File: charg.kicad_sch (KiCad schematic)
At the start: 21 parts, among them J1 Vbus, J2 GND, J3 Vout, J4 EN, Q1 FDC610PZ

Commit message: fixes
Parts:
- removed BT1: Battery_Cell, symbol Device:Battery_Cell
- added J?: Vbatt, symbol Connector_Generic:Conn_01x01
- C3, C5: footprint (none) -> capa 10uf:CAPAE530X610N
- TH1: footprint (none) -> Button_Switch_THT:KSA_Tactile_SPST
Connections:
- net at Battery_Charger_IC1.10 (BAT), C5.1, L1.2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: now also J?.1 (Pin_1)
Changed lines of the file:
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@@
   (junction (at 92.71 118.11) (diameter 0) (color 0 0 0 0)
   )
-  (junction (at 109.22 104.14) (diameter 0) (color 0 0 0 0)
-  )
-  (junction (at 194.31 114.3) (diameter 0) (color 0 0 0 0)
-  )
   (junction (at 102.87 104.14) (diameter 0) (color 0 0 0 0)
   )
@@
     (stroke (width 0) (type default) (color 0 0 0 0))
   )
-  (wire (pts (xy 194.31 111.76) (xy 194.31 114.3))
-    (stroke (width 0) (type default) (color 0 0 0 0))
-  )
   (wire (pts (xy 175.26 80.01) (xy 181.61 80.01))
     (stroke (width 0) (type default) (color 0 0 0 0))
@@
     (stroke (width 0) (type default) (color 0 0 0 0))
   )
-  (wire (pts (xy 113.03 104.14) (xy 109.22 104.14))
-    (stroke (width 0) (type default) (color 0 0 0 0))
-  )
   (wire (pts (xy 139.7 121.92) (xy 139.7 124.46))
     (stroke (width 0) (type default) (color 0 0 0 0))
@@
     (stroke (width 0) (type default) (color 0 0 0 0))
   )
-  (wire (pts (xy 180.34 100.33) (xy 180.34 104.14))
+  (wire (pts (xy 180.34 102.87) (xy 180.34 104.14))
     (stroke (width 0) (type default) (color 0 0 0 0))
   )
@@
     (stroke (width 0) (type default) (color 0 0 0 0))
   )
-  (wire (pts (xy 172.72 124.46) (xy 172.72 100.33))
+  (wire (pts (xy 172.72 124.46) (xy 172.72 102.87))
     (stroke (width 0) (type default) (color 0 0 0 0))
   )
@@
     (stroke (width 0) (type default) (color 0 0 0 0))
   )
-  (wire (pts (xy 194.31 104.14) (xy 194.31 96.52))
-    (stroke (width 0) (type default) (color 0 0 0 0))
-  )
-  (wire (pts (xy 172.72 100.33) (xy 180.34 100.33))
+  (wire (pts (xy 172.72 102.87) (xy 180.34 102.87))
     (stroke (width 0) (type default) (color 0 0 0 0))
   )
@@
       (effects (font (size 1.27 1.27)) (justify left))
     )
-    (property "Footprint" "" (id 2) (at 102.5652 73.66 0)
+    (property "Footprint" "capa 10uf:CAPAE530X610N" (id 2) (at 102.5652 73.66 0)
       (effects (font (size 1.27 1.27)) hide)
     )
@@
       (effects (font (size 1.27 1.27)) (justify left))
     )
-    (property "Footprint" "" (id 2) (at 180.34 109.22 0)
+    (property "Footprint" "Button_Switch_THT:KSA_Tactile_SPST" (id 2) (at 180.34 109.22 0)
       (effects (font (size 1.27 1.27)) hide)
     )
@@
     (pin "1")
     (pin "2")
+  )
+  (symbol (lib_name "Conn_01x01_2") (lib_id "Connector_Generic:Conn_01x01") (at 199.39 96.52 0) (unit 1)
+    (in_bom yes) (on_board yes)
+    (property "Reference" "J?" (id 0) (at 201.93 95.2499 0)
+      (effects (font (size 1.27 1.27)) (justify left) hide)
+    )
+    (property "Value" "Vbatt" (id 1) (at 203.2 96.52 0)
+      (effects (font (size 1.27 1.27)) (justify left))
+    )
+    (property "Footprint" "" (id 2) (at 199.39 96.52 0)
+      (effects (font (size 1.27 1.27)) hide)
+    )
+    (property "Datasheet" "~" (id 3) (at 199.39 96.52 0)
+      (effects (font (size 1.27 1.27)) hide)
+    )
+    (pin "1")
   )
   (symbol (lib_id "Device:C") (at 102.87 110.49 0) (unit 1)
@@
       (effects (font (size 1.27 1.27)) (justify left))
     )
-    (property "Footprint" "" (id 2) (at 182.5752 87.63 0)
+    (property "Footprint" "capa 10uf:CAPAE530X610N" (id 2) (at 182.5752 87.63 0)
       (effects (font (size 1.27 1.27)) hide)
     )
@@
     (pin "2")
   )
-  (symbol (lib_id "Device:Battery_Cell") (at 194.31 109.22 0) (unit 1)
-    (in_bom yes) (on_board yes)
-    (property "Reference" "BT1" (id 0) (at 198.12 105.9179 0)
-      (effects (font (size 1.27 1.27)) (justify left))
-    )
-    (property "Value" "Battery_Cell" (id 1) (at 196.85 109.22 0)
-      (effects (font (size 1.27 1.27)) (justify left))
-    )
-    (property "Footprint" "" (id 2) (at 194.31 107.696 90)
-      (effects (font (size 1.27 1.27)) hide)
-    )
-    (property "Datasheet" "~" (id 3) (at 194.31 107.696 90)
-      (effects (font (size 1.27 1.27)) hide)
-    )
-    (pin "1")
-    (pin "2")
-  )
   (symbol (lib_name "Conn_01x01_1") (lib_id "Connector_Generic:Conn_01x01") (at 86.36 118.11 180) (unit 1)
     (in_bom yes) (on_board yes)
@@
       (reference "#PWR?") (unit 1) (value "Earth") (footprint "")
     )
-    (path "/9ba9fbab-7f8a-40ec-b6d6-6779dc40ce87"
-      (reference "BT1") (unit 1) (value "Battery_Cell") (footprint "")
-    )
     (path "/0f9df193-831e-47d8-a0ce-da7d0c29948d"
       (reference "Battery_Charger_IC1") (unit 1) (value "BQ25302RTER") (footprint "QFN50P300X300X80-17N-D")
@@
     )
     (path "/2ee2590c-9ec5-4299-aea1-5cf0b3e9f0eb"
-      (reference "C3") (unit 1) (value "10uF") (footprint "")
+      (reference "C3") (unit 1) (value "10uF") (footprint "capa 10uf:CAPAE530X610N")
     )
     (path "/8c8e53e9-f812-4cae-9967-ee70b6bcdceb"
@@
     )
     (path "/654041ef-084b-4054-b478-8dfb24f82083"
-      (reference "C5") (unit 1) (value "10uF") (footprint "")
+      (reference "C5") (unit 1) (value "10uF") (footprint "capa 10uf:CAPAE530X610N")
     )
     (path "/e76b96cb-2d62-4d86-a100-3adc0aa0ebaa"
@@
       (reference "J?") (unit 1) (value "GND") (footprint "")
     )
+    (path "/4c166f5d-fc04-4737-b218-6d3749f4fb20"
+      (reference "J?") (unit 1) (value "Vbatt") (footprint "")
+    )
     (path "/d224ad5a-0553-4678-9e65-20c886863dd5"
       (reference "L1") (unit 1) (value "0.058uH") (footprint "")
@@
     )
     (path "/4506fe3c-6f6a-4c6d-8eb9-7a507a5f2f0f"
-      (reference "TH1") (unit 1) (value "103AT-2 Thermistor") (footprint "")
-    )
-  )
+      (reference "TH1") (unit 1) (value "103AT-2 Thermistor") (footprint "Button_Switch_THT:KSA_Tactile_SPST")
+    )
+  )

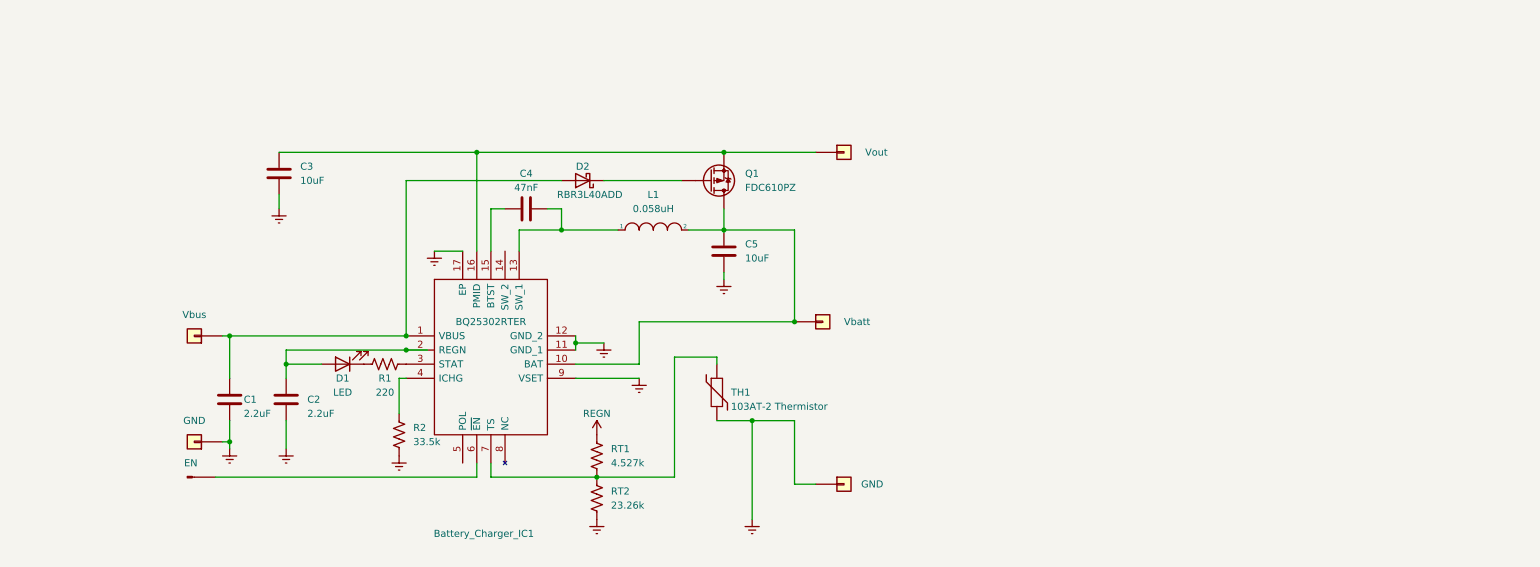
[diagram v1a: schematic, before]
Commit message: Major schematic edit
Thermy and STAT LED should be connected externally. Assigned FPs.
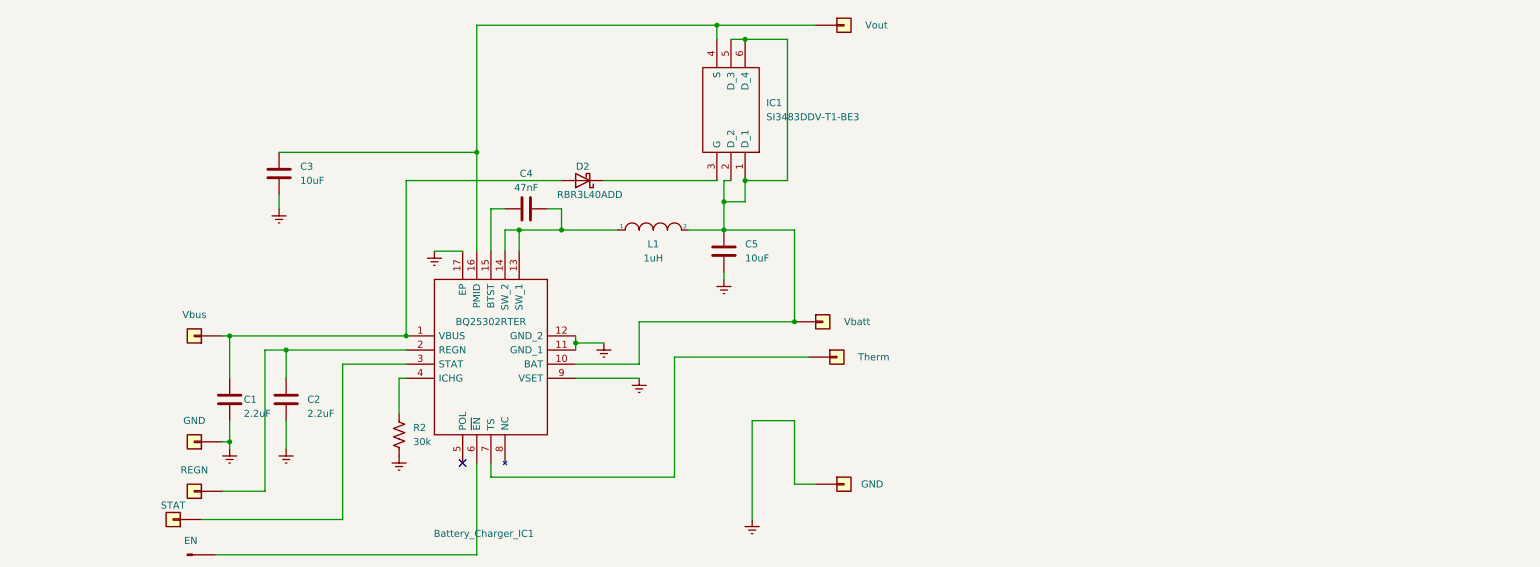
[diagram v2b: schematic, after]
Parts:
- removed D1: LED, symbol Device:LED
- removed Q1: FDC610PZ, Package_SO:TSOP-6_1.65x3.05mm_P0.95mm, symbol Transistor_FET:PMN48XP
- removed R1: 220, symbol Device:R_US
- removed RT1: 4.527k, symbol Device:R_US
- removed RT2: 23.26k, symbol Device:R_US
- removed TH1: 103AT-2 Thermistor, Button_Switch_THT:KSA_Tactile_SPST, symbol Device:Thermistor
- added IC1: SI3483DDV-T1-BE3, SOT95P284X110-6N, symbol PFET SI3483DDV-T1-BE3:SI3483DDV-T1-BE3
- added J6: Therm, TerminalBlock_MetzConnect:TerminalBlock_MetzConnect_360271_1x01_Horizontal_ScrewM3.0_Boxed, symbol Connector_Generic:Conn_01x01
- added J?: REGN, TerminalBlock_MetzConnect:TerminalBlock_MetzConnect_360271_1x01_Horizontal_ScrewM3.0_Boxed, symbol Connector_Generic:Conn_01x01
- added J?: STAT, TerminalBlock_MetzConnect:TerminalBlock_MetzConnect_360271_1x01_Horizontal_ScrewM3.0_Boxed, symbol Connector_Generic:Conn_01x01
- C1, C2: footprint (none) -> 2.2uF:CAPC0603X33N
- C4: footprint (none) -> 47nF:C1005_Commercial
- D2: footprint (none) -> Schottky dd:DIOM5026X220N
- J1, J2, J3: footprint (none) -> TerminalBlock_MetzConnect:TerminalBlock_MetzConnect_360271_1x01_Horizontal_ScrewM3.0_Boxed
- J4: footprint (none) -> Connector_PinHeader_1.00mm:PinHeader_1x01_P1.00mm_Vertical
- J5, J7: renamed from J?; footprint (none) -> TerminalBlock_MetzConnect:TerminalBlock_MetzConnect_360271_1x01_Horizontal_ScrewM3.0_Boxed
- L1: value 0.058uH -> 1uH; footprint (none) -> 1uH indc:IHHP0805ZHER1R0M01
- R2: value 33.5k -> 30k; footprint (none) -> 30k rst:RESC2012X70N
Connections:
- net at Battery_Charger_IC1.3 (STAT): now also J?.1 (Pin_1)
- net at Battery_Charger_IC1.16 (PMID), C3.1, J3.1 (Pin_1): now also IC1.4 (S)
- net at Battery_Charger_IC1.10 (BAT), C5.1, J5.1 (Pin_1)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: now also IC1.1 (D_1), IC1.2 (D_2), IC1.5 (D_3), IC1.6 (D_4)
- net at Battery_Charger_IC1.13 (SW_1), C4.2, L1.1: now also Battery_Charger_IC1.14 (SW_2)
- net at Battery_Charger_IC1.2 (REGN), C2.1: now also J?.1 (Pin_1)
- net at Battery_Charger_IC1.7 (TS): now also J6.1 (Pin_1)
- net at D2.1 (K): now also IC1.3 (G)
- no-connect marks 0 -> 1

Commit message: Patches + PCB start
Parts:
- C3, C5: footprint capa 10uf:CAPAE530X610N -> 10uF MLCC:CAPC2012X94N
- IC1: footprint SOT95P284X110-6N -> PFET:SOT95P284X110-6N
- IC2: renamed from Battery_Charger_IC1; footprint QFN50P300X300X80-17N-D -> Charger bq 25302:QFN50P300X300X80-17N-D
- gave numbers to parts that had none: 2
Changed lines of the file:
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@@
   (symbol (lib_id "batt ch:BQ25302RTER") (at 124.46 99.06 0) (unit 1)
     (in_bom yes) (on_board yes)
-    (property "Reference" "Battery_Charger_IC1" (id 0) (at 138.43 134.62 0))
+    (property "Reference" "IC2" (id 0) (at 139.7 102.87 0))
     (property "Value" "BQ25302RTER" (id 1) (at 139.7 96.52 0))
-    (property "Footprint" "QFN50P300X300X80-17N-D" (id 2) (at 151.13 88.9 0)
+    (property "Footprint" "Charger bq 25302:QFN50P300X300X80-17N-D" (id 2) (at 151.13 88.9 0)
       (effects (font (size 1.27 1.27)) (justify left) hide)
     )
@@
       (effects (font (size 1.27 1.27)) (justify left))
     )
-    (property "Footprint" "capa 10uf:CAPAE530X610N" (id 2) (at 102.5652 73.66 0)
+    (property "Footprint" "10uF MLCC:CAPC2012X94N" (id 2) (at 102.5652 73.66 0)
       (effects (font (size 1.27 1.27)) hide)
     )
@@
   (symbol (lib_id "Connector_Generic:Conn_01x01") (at 86.36 127 180) (unit 1)
     (in_bom yes) (on_board yes) (fields_autoplaced)
-    (property "Reference" "J?" (id 0) (at 86.36 120.65 0)
+    (property "Reference" "J9" (id 0) (at 86.36 120.65 0)
       (effects (font (size 1.27 1.27)) hide)
     )
@@
       (effects (font (size 1.27 1.27)) (justify left))
     )
-    (property "Footprint" "capa 10uf:CAPAE530X610N" (id 2) (at 182.5752 87.63 0)
+    (property "Footprint" "10uF MLCC:CAPC2012X94N" (id 2) (at 182.5752 87.63 0)
       (effects (font (size 1.27 1.27)) hide)
     )
@@
   (symbol (lib_id "Connector_Generic:Conn_01x01") (at 82.55 132.08 180) (unit 1)
     (in_bom yes) (on_board yes)
-    (property "Reference" "J?" (id 0) (at 82.55 125.73 0)
+    (property "Reference" "J8" (id 0) (at 82.55 125.73 0)
       (effects (font (size 1.27 1.27)) hide)
     )
@@
       (effects (font (size 1.27 1.27)) (justify left))
     )
-    (property "Footprint" "SOT95P284X110-6N" (id 2) (at 187.96 49.53 0)
+    (property "Footprint" "PFET:SOT95P284X110-6N" (id 2) (at 187.96 49.53 0)
       (effects (font (size 1.27 1.27)) (justify left) hide)
     )
@@
       (reference "#PWR010") (unit 1) (value "Earth") (footprint "")
     )
-    (path "/0f9df193-831e-47d8-a0ce-da7d0c29948d"
-      (reference "Battery_Charger_IC1") (unit 1) (value "BQ25302RTER") (footprint "QFN50P300X300X80-17N-D")
-    )
     (path "/b9a740b3-1199-4755-a81b-90abafe42fd7"
       (reference "C1") (unit 1) (value "2.2uF") (footprint "2.2uF:CAPC0603X33N")
@@
     )
     (path "/2ee2590c-9ec5-4299-aea1-5cf0b3e9f0eb"
-      (reference "C3") (unit 1) (value "10uF") (footprint "capa 10uf:CAPAE530X610N")
+      (reference "C3") (unit 1) (value "10uF") (footprint "10uF MLCC:CAPC2012X94N")
     )
     (path "/8c8e53e9-f812-4cae-9967-ee70b6bcdceb"
@@
     )
     (path "/654041ef-084b-4054-b478-8dfb24f82083"
-      (reference "C5") (unit 1) (value "10uF") (footprint "capa 10uf:CAPAE530X610N")
+      (reference "C5") (unit 1) (value "10uF") (footprint "10uF MLCC:CAPC2012X94N")
     )
     (path "/64e04f30-b75a-485a-9e25-e618219d18d5"
@@
     )
     (path "/ff90fce7-88c8-4858-850a-5a7e1e5af2e0"
-      (reference "IC1") (unit 1) (value "SI3483DDV-T1-BE3") (footprint "SOT95P284X110-6N")
+      (reference "IC1") (unit 1) (value "SI3483DDV-T1-BE3") (footprint "PFET:SOT95P284X110-6N")
+    )
+    (path "/0f9df193-831e-47d8-a0ce-da7d0c29948d"
+      (reference "IC2") (unit 1) (value "BQ25302RTER") (footprint "Charger bq 25302:QFN50P300X300X80-17N-D")
     )
     (path "/79fa7dca-d77d-4145-9ff2-23d1227b0ff9"
@@
       (reference "J7") (unit 1) (value "GND") (footprint "TerminalBlock_MetzConnect:TerminalBlock_MetzConnect_360271_1x01_Horizontal_ScrewM3.0_Boxed")
     )
+    (path "/7e0cd443-1a33-424f-98d1-87219868fdec"
+      (reference "J8") (unit 1) (value "STAT") (footprint "TerminalBlock_MetzConnect:TerminalBlock_MetzConnect_360271_1x01_Horizontal_ScrewM3.0_Boxed")
+    )
     (path "/36f5e256-8a62-4fe6-8298-ccddfb01e790"
-      (reference "J?") (unit 1) (value "REGN") (footprint "TerminalBlock_MetzConnect:TerminalBlock_MetzConnect_360271_1x01_Horizontal_ScrewM3.0_Boxed")
-    )
-    (path "/7e0cd443-1a33-424f-98d1-87219868fdec"
-      (reference "J?") (unit 1) (value "STAT") (footprint "TerminalBlock_MetzConnect:TerminalBlock_MetzConnect_360271_1x01_Horizontal_ScrewM3.0_Boxed")
+      (reference "J9") (unit 1) (value "REGN") (footprint "TerminalBlock_MetzConnect:TerminalBlock_MetzConnect_360271_1x01_Horizontal_ScrewM3.0_Boxed")
     )
     (path "/d224ad5a-0553-4678-9e65-20c886863dd5"

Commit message: Debloat
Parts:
- removed J1: Vbus, TerminalBlock_MetzConnect:TerminalBlock_MetzConnect_360271_1x01_Horizontal_ScrewM3.0_Boxed, symbol Connector_Generic:Conn_01x01
- removed J2, J7: GND, TerminalBlock_MetzConnect:TerminalBlock_MetzConnect_360271_1x01_Horizontal_ScrewM3.0_Boxed, symbol Connector_Generic:Conn_01x01
- removed J3: Vout, TerminalBlock_MetzConnect:TerminalBlock_MetzConnect_360271_1x01_Horizontal_ScrewM3.0_Boxed, symbol Connector_Generic:Conn_01x01
- removed J5: Vbatt, TerminalBlock_MetzConnect:TerminalBlock_MetzConnect_360271_1x01_Horizontal_ScrewM3.0_Boxed, symbol Connector_Generic:Conn_01x01
- removed J6: Therm, TerminalBlock_MetzConnect:TerminalBlock_MetzConnect_360271_1x01_Horizontal_ScrewM3.0_Boxed, symbol Connector_Generic:Conn_01x01
- removed J8: STAT, TerminalBlock_MetzConnect:TerminalBlock_MetzConnect_360271_1x01_Horizontal_ScrewM3.0_Boxed, symbol Connector_Generic:Conn_01x01
- removed J9: REGN, TerminalBlock_MetzConnect:TerminalBlock_MetzConnect_360271_1x01_Horizontal_ScrewM3.0_Boxed, symbol Connector_Generic:Conn_01x01
- added J1, J2: Screw_Terminal_01x04, Boost LTC3426:TerminalBlock_MetzConnect_Type059_RT06304HBWC_1x04_P3.50mm_Horizontal, symbol Connector:Screw_Terminal_01x04
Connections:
- net Earth: now also J1.2 (Pin_2), J2.4 (Pin_4)
- net at C3.1, IC1.4 (S), IC2.16 (PMID): now also J2.1 (Pin_1)
- net at C1.1, D2.2 (A), IC2.1 (VBUS): now also J1.1 (Pin_1)
- net at C5.1, IC1.1 (D_1), IC1.2 (D_2)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: now also J2.2 (Pin_2)
- net at C2.1, IC2.2 (REGN): now also J1.3 (Pin_3)
- net at IC2.3 (STAT): now also J1.4 (Pin_4)
- net at IC2.7 (TS): now also J2.3 (Pin_3)
